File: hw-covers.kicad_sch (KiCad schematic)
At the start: 110 parts, among them J1 Screw_Terminal_01x02, J2 Screw_Terminal_01x10, J3 Conn_01x04_Pin, J4 Conn_01x04_Pin, J5 Screw_Terminal_01x15, K1 JRC-21F(4100), K10 JRC-21F(4100), K2 JRC-21F(4100), K3 JRC-21F(4100), K4 JRC-21F(4100), K5 JRC-21F(4100), K6 JRC-21F(4100), K7 JRC-21F(4100), K8 JRC-21F(4100), K9 JRC-21F(4100), Q1 PMBT3904235, Q10 PMBT3904235, Q11 PMBT3904235, Q2 PMBT3904235, Q3 PMBT3904235, Q4 PMBT3904235, Q5 PMBT3904235, Q6 PMBT3904235, Q7 PMBT3904235, Q8 PMBT3904235, Q9 PMBT3904235, SW1 SW_Push, U2 NCP1117-3.3_SOT223, U3 HLK-2M05, U4 ESP32-S3-WROOM-1

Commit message: Release 1.0
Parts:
- removed D14: LED, LED_THT:LED_D5.0mm, symbol Device:LED
- removed J1: Screw_Terminal_01x02, Connector_Phoenix_MSTB:PhoenixContact_MSTBA_2,5_2-G_1x02_P5.00mm_Horizontal, symbol Connector:Screw_Terminal_01x02
- removed J2: Screw_Terminal_01x10, Connector_Phoenix_MSTB:PhoenixContact_MSTBA_2,5_10-G_1x10_P5.00mm_Horizontal, symbol Connector:Screw_Terminal_01x10
- removed J5: Screw_Terminal_01x15, Connector_Phoenix_MC:PhoenixContact_MC_1,5_15-G-3.81_1x15_P3.81mm_Horizontal, symbol Connector:Screw_Terminal_01x15
- removed U4: ESP32-S3-WROOM-1, RF_Module:ESP32-S3-WROOM-1, symbol RF_Module:ESP32-S3-WROOM-1
- added J1, J2, J7: Screw_Terminal_01x04, Connector_Phoenix_MSTB:PhoenixContact_MSTBA_2,5_4-G-5,08_1x04_P5.08mm_Horizontal, symbol Connector:Screw_Terminal_01x04
- added J10, J11, J5, J8, J9: Screw_Terminal_01x03, Connector_Phoenix_MC:PhoenixContact_MC_1,5_3-G-3.81_1x03_P3.81mm_Horizontal, symbol Connector:Screw_Terminal_01x03
- added J6: Conn_01x02_Pin, Connector_PinHeader_2.54mm:PinHeader_1x02_P2.54mm_Vertical, symbol Connector:Conn_01x02_Pin
- added TP1, TP2: TestPoint, TestPoint:TestPoint_Pad_D1.5mm, symbol Connector:TestPoint
- added U1: ESP32-S3-WROOM-1, guille-lib:ESP32-S3-WROOM-1, symbol guille-lib:ESP32-S3-WROOM-1
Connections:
- net +3V3: now also U1.2 (3V3)
- net 1IN1: now also U1.22 (IO14)
- net 1IN2: now also U1.23 (IO21)
- net 1OUT1: now also U1.9 (IO16)
- net 1OUT2: now also U1.10 (IO17)
- net 2IN1: now also U1.24 (IO47)
- net 2IN2: now also U1.25 (IO48)
- net 2OUT1: now also U1.11 (IO18)
- net 2OUT2: now also U1.12 (IO8)
- net 3IN1: now also U1.32 (IO39)
- net 3IN2: now also U1.33 (IO40)
- net 3OUT1: now also U1.13 (USB_D-)
- net 3OUT2: now also U1.14 (USB_D+)
- net 4IN1: now also U1.34 (IO41)
- net 4IN2: now also U1.35 (IO42)
- net 4OUT1: now also U1.17 (IO9)
- net 4OUT2: now also U1.18 (IO10)
- net 5IN1: now also U1.38 (IO2)
- net 5IN2: now also U1.39 (IO1)
- net 5OUT1: now also U1.19 (IO11)
- net 5OUT2: now also U1.20 (IO12)
- net ESP_IO0: now also U1.27 (IO0)
- net ESP_RX: now also J4.2 (Pin_2), U1.36 (RXD0); no longer J4.3 (Pin_3)
- net ESP_TX: now also J4.3 (Pin_3), U1.37 (TXD0); no longer J4.2 (Pin_2)
- net EXT1: now also U1.5 (IO5)
- net EXT2: now also U1.4 (IO4)
- net GND: now also J10.3 (Pin_3), J11.3 (Pin_3), J5.3 (Pin_3), J8.3 (Pin_3), J9.3 (Pin_3), U1.1 (GND), U1.40 (GND), U1.41 (GND)
- net IN1_DOWN: now also J5.2 (Pin_2)
- net IN1_UP: now also J5.1 (Pin_1)
- net IN2_DOWN: now also J8.2 (Pin_2)
- net IN2_UP: now also J8.1 (Pin_1)
- net IN3_DOWN: now also J9.2 (Pin_2)
- net IN3_UP: now also J9.1 (Pin_1)
- net IN4_DOWN: now also J10.2 (Pin_2)
- net IN4_UP: now also J10.1 (Pin_1)
- net IN5_DOWN: now also J11.2 (Pin_2)
- net IN5_UP: now also J11.1 (Pin_1)
- net IR: now also U1.6 (IO6)
- net L: now also J2.4 (Pin_4)
- net LED1: now also U1.8 (IO15)
- net LED2: now also U1.7 (IO7)
- net N: now also J2.3 (Pin_3)
- net OUT1_DOWN: now also J7.2 (Pin_2)
- net OUT1_UP: now also J7.1 (Pin_1)
- net OUT2_DOWN: now also J7.4 (Pin_4)
- net OUT2_UP: now also J7.3 (Pin_3)
- net OUT3_DOWN: now also J1.2 (Pin_2)
- net OUT3_UP: now also J1.1 (Pin_1)
- net OUT4_DOWN: now also J1.4 (Pin_4)
- net OUT4_UP: now also J1.3 (Pin_3)
- net OUT5_DOWN: now also J2.2 (Pin_2)
- net OUT5_UP: now also J2.1 (Pin_1)
- net at R4.1: now also U1.3 (EN)
- net at Q11.3: now also J6.2 (Pin_2)
- net at R17.2: now also J6.1 (Pin_1)
- new net: TP1.1, U1.21 (IO13)
- new net: TP2.1, U1.31 (IO38)
- no-connect marks 22 -> 20
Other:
- company: (none) -> Guille González
- title: (none) -> Covers
- moved on the sheet: Q11, R17

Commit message: Release 1.1
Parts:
- removed K1, K10, K2, K3, K4, K5, K6, K7, K8, K9: JRC-21F(4100), guille-lib:JRC-21F(4100), symbol guille-lib:JRC-21F(4100)
- removed R16: 1k, Resistor_SMD:R_0402_1005Metric, symbol Device:R
- removed U3: HLK-2M05, guille-lib:HLK-2M05, symbol guille-lib:HLK-2M05
- added K1, K10, K2, K3, K4, K5, K6, K7, K8, K9: HF46F, guille-lib:HF46F, symbol guille-lib:HF46F
- added PS1: HLK-2M05, Converter_ACDC:Converter_ACDC_Hi-Link_HLK-2Mxx, symbol Converter_ACDC:HLK-2M05
- added R5: 1k, Resistor_SMD:R_0603_1608Metric, symbol Device:R
- C1, C2: footprint Capacitor_SMD:C_1206_3216Metric -> Capacitor_SMD:C_0805_2012Metric
- C10, C11, C12, C13, C14, C4, C5, C6, C7, C8, C9: footprint Capacitor_SMD:C_0402_1005Metric -> Capacitor_SMD:C_0603_1608Metric
- D1, D10, D11, D12, D13, D2, D6, D7, D8, D9: footprint Diode_SMD:D_SOD-323 -> Diode_SMD:D_SOD-123
- R1, R10, R11, R12, R13, R14, R15, R18, R19, R2, R20, R21, R22, R23, R24, R25, R26, R27, R28, R29, R3, R30, R31, R32, R33, R34, R35, R36, R37, R4, R9: footprint Resistor_SMD:R_0402_1005Metric -> Resistor_SMD:R_0603_1608Metric
- R17: value 1k -> 180; footprint Resistor_SMD:R_0402_1005Metric -> Resistor_SMD:R_0603_1608Metric
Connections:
- net +5V: now also K1.4, K10.4, K2.4, K3.4, K4.4, K5.4, K6.4, K7.4, K8.4, K9.4, PS1.4 (+Vout)
- net 1OUT1: now also U1.18 (IO10); no longer U1.9 (IO16)
- net 1OUT2: now also R1.1, U1.17 (IO9); no longer R9.1, U1.10 (IO17)
- net 2OUT1: now also U1.14 (USB_D+), R5.1; no longer R1.1, U1.11 (IO18)
- net 2OUT2: now also R9.1, U1.13 (USB_D-); no longer R10.1, U1.12 (IO8)
- net 3OUT1: now also R10.1, U1.12 (IO8); no longer R11.1, U1.13 (USB_D-)
- net 3OUT2: now also R11.1, U1.11 (IO18); no longer R13.1, U1.14 (USB_D+)
- net 4OUT1: now also U1.10 (IO17); no longer U1.17 (IO9)
- net 4OUT2: now also R13.1, U1.9 (IO16); no longer R14.1, U1.18 (IO10)
- net 5OUT1: now also R14.1, U1.8 (IO15); no longer R15.1, U1.19 (IO11)
- net 5OUT2: now also R15.1, U1.7 (IO7); no longer U1.20 (IO12)
- net GND: now also PS1.3 (-Vout)
- net LED1: now also U1.19 (IO11); no longer U1.8 (IO15)
- net LED2: now also U1.20 (IO12); no longer U1.7 (IO7)
- net LF: now also K1.2, K10.2, K2.2, K3.2, K4.2, K5.2, K6.2, K7.2, K8.2, K9.2, PS1.1 (AC/L)
- net N: now also PS1.2 (AC/N)
- net OUT1_DOWN: now also J2.1 (Pin_1), K2.1; no longer J7.2 (Pin_2)
- net OUT1_UP: now also J2.2 (Pin_2), K1.1; no longer J7.1 (Pin_1)
- net OUT2_DOWN: now also J1.3 (Pin_3), K4.1; no longer J7.4 (Pin_4)
- net OUT2_UP: now also J1.4 (Pin_4), K3.1; no longer J7.3 (Pin_3)
- net OUT3_DOWN: now also J1.1 (Pin_1), K6.1; no longer J1.2 (Pin_2)
- net OUT3_UP: now also J1.2 (Pin_2), K5.1; no longer J1.1 (Pin_1)
- net OUT4_DOWN: now also J7.3 (Pin_3), K8.1; no longer J1.4 (Pin_4)
- net OUT4_UP: now also J7.4 (Pin_4), K7.1; no longer J1.3 (Pin_3)
- net OUT5_DOWN: now also J7.1 (Pin_1), K10.1; no longer J2.2 (Pin_2)
- net OUT5_UP: now also J7.2 (Pin_2), K9.1; no longer J2.1 (Pin_1)
- net at D2.2 (A), Q1.3: now also K1.3
- net at R9.2: now also Q4.1; no longer Q3.1
- net at D6.2 (A), Q3.3: now also K3.3
- net at Q10.1: now also R15.2
- net at D13.2 (A), Q10.3: now also K10.3
- net at Q6.1: now also R11.2; no longer R12.2
- net at Q9.1: now also R14.2; no longer R15.2
- net at D12.2 (A), Q9.3: now also K9.3
- net at Q5.1: now also R10.2; no longer R11.2
- net at D7.2 (A), Q4.3: now also K4.3
- net at D1.2 (A), Q2.3: now also K2.3
- net at Q8.1: now also R13.2; no longer R14.2
- net at D9.2 (A), Q6.3: now also K6.3
- net at Q7.1: now also R12.2; no longer R13.2
- net at D8.2 (A), Q5.3: now also K5.3
- net at D10.2 (A), Q7.3: now also K7.3
- net at D11.2 (A), Q8.3: now also K8.3
- new net: Q3.1, R5.2
- no-connect marks 20 -> 10
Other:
- note added: "R LED_IR: (5V-1.5V)/20mA = 175ohm 180ohm (commercial)"
- note removed: "TBD"
- moved on the sheet: D2, H1, H2, H3, H4, Q1, R2

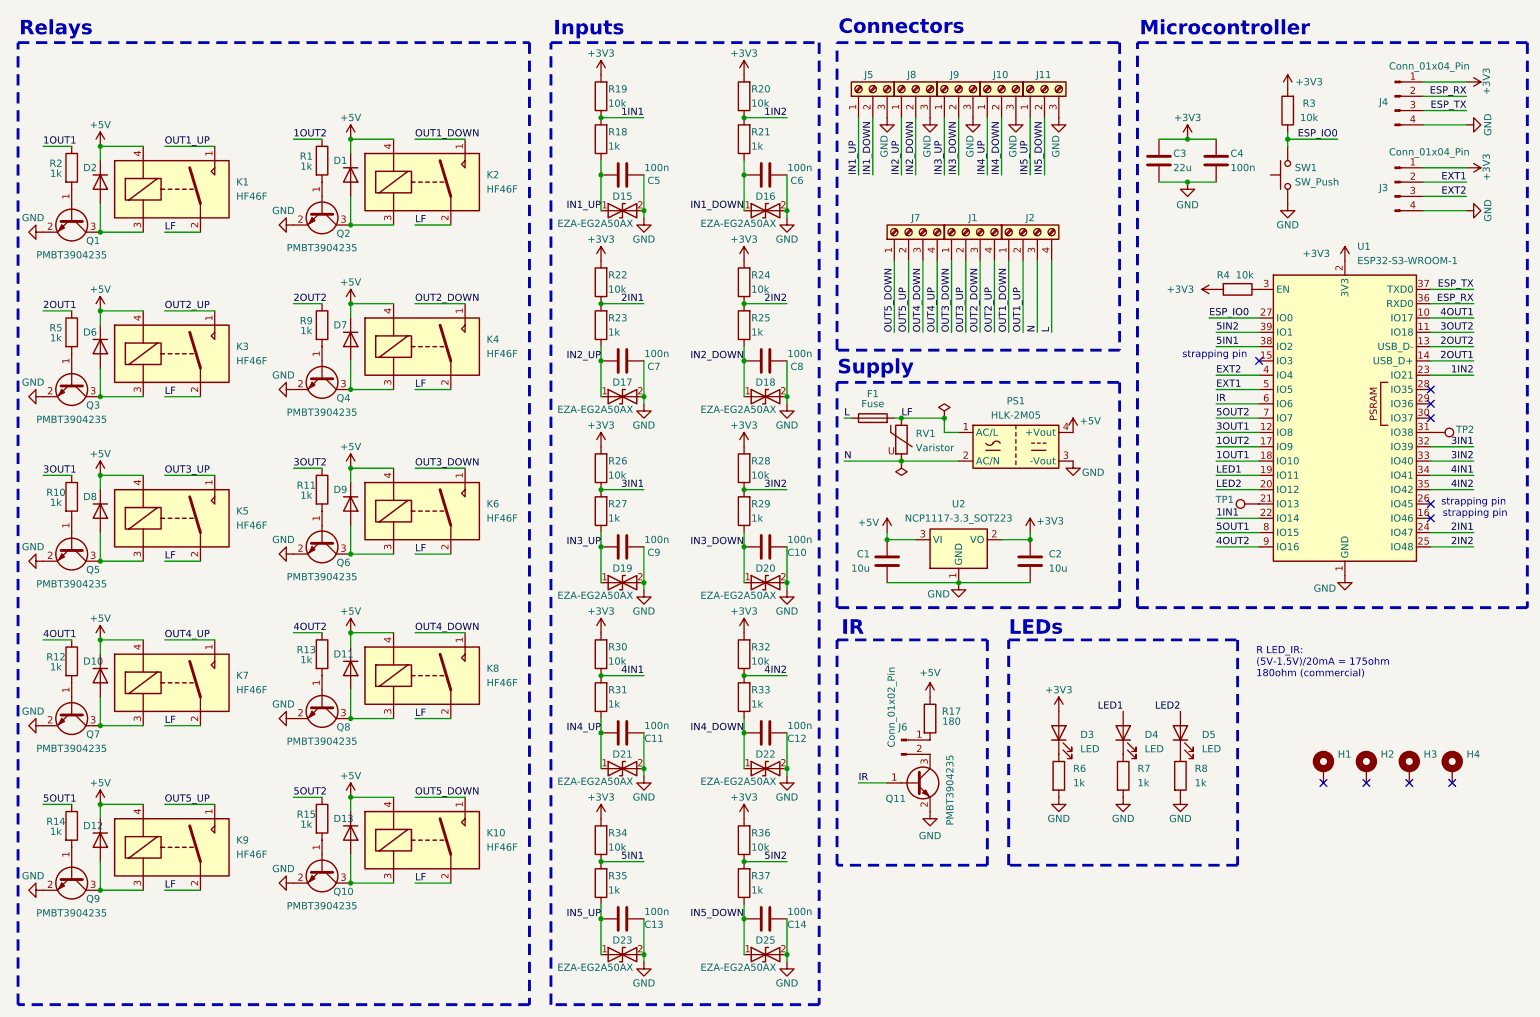
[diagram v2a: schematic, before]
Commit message: Sch update for rev 2
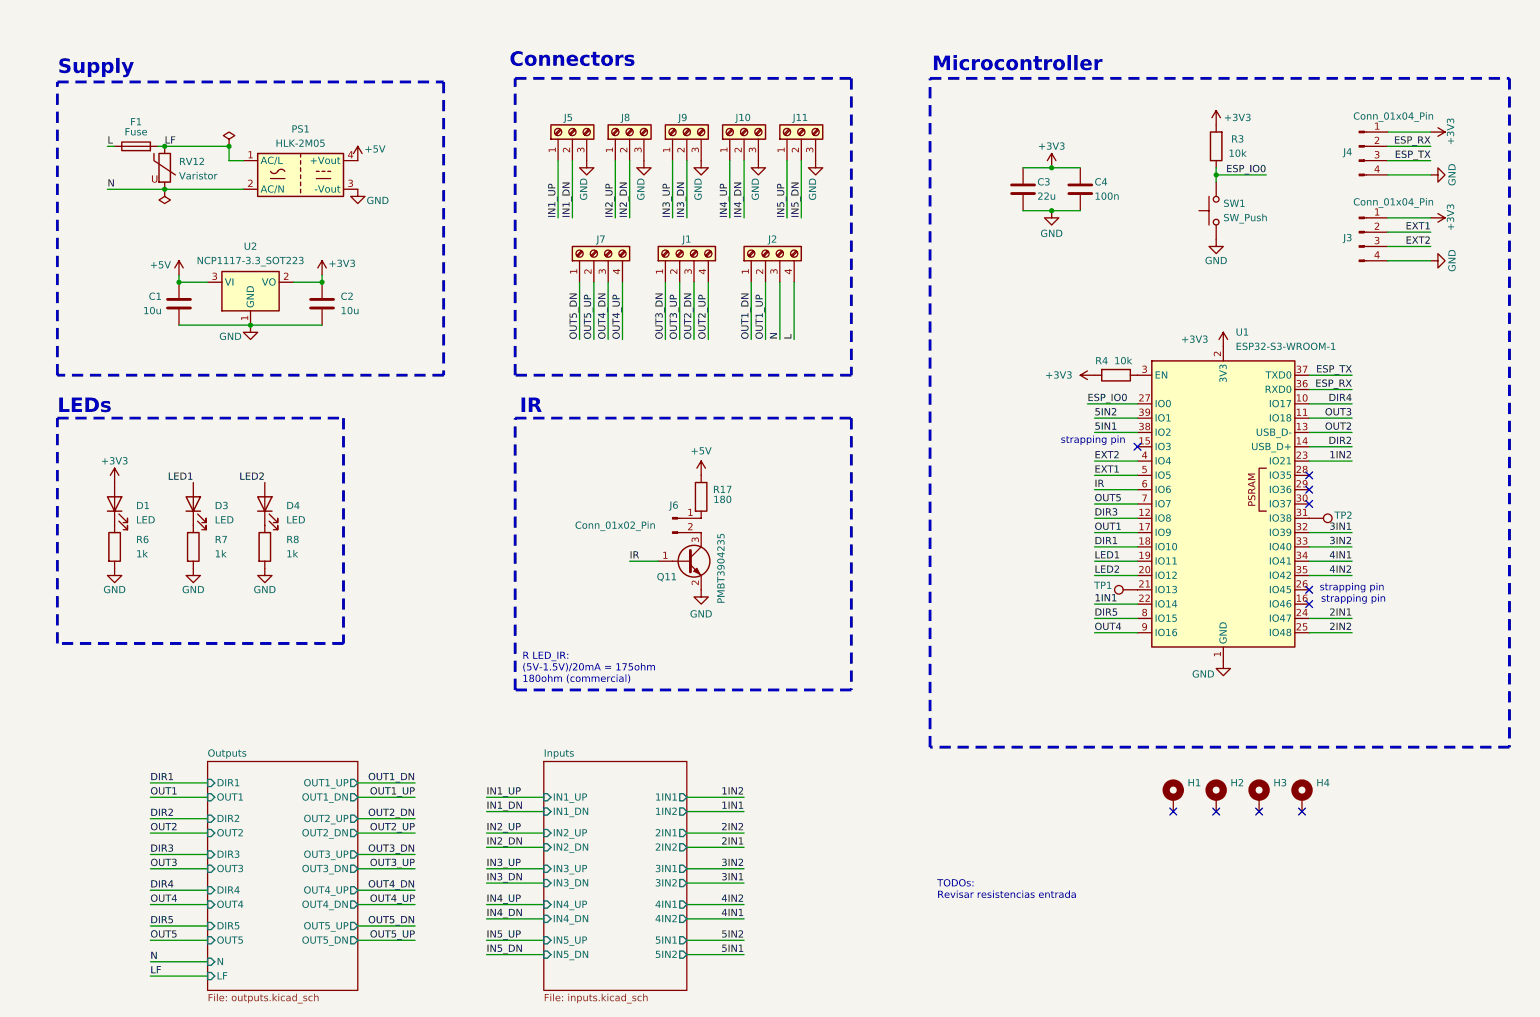
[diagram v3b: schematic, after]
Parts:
- removed C10, C11, C12, C13, C14, C5, C6, C7, C8, C9: 100n, Capacitor_SMD:C_0603_1608Metric, symbol Device:C
- removed D1, D10, D11, D12, D13, D2, D6, D7, D8, D9: 1N4448W, Diode_SMD:D_SOD-123, symbol Device:D
- removed D15, D16, D17, D18, D19, D20, D21, D22, D23, D25: EZA-EG2A50AX, guille-lib:EZAEG2A50AX, symbol guille-lib:EZA-EG2A50AX
- removed D5: LED, LED_SMD:LED_0603_1608Metric, symbol Device:LED
- removed K1, K10, K2, K3, K4, K5, K6, K7, K8, K9: HF46F, guille-lib:HF46F, symbol guille-lib:HF46F
- removed Q1, Q10, Q2, Q3, Q4, Q5, Q6, Q7, Q8, Q9: PMBT3904235, Package_TO_SOT_SMD:SOT-23, symbol guille-lib:PMBT3904235
- removed R1, R10, R11, R12, R13, R14, R15, R18, R2, R21, R23, R25, R27, R29, R31, R33, R35, R37, R5, R9: 1k, Resistor_SMD:R_0603_1608Metric, symbol Device:R
- removed R19, R20, R22, R24, R26, R28, R30, R32, R34, R36: 10k, Resistor_SMD:R_0603_1608Metric, symbol Device:R
- removed RV1: Varistor, Varistor:RV_Disc_D12mm_W4.5mm_P7.5mm, symbol Device:Varistor
- added D1: LED, LED_SMD:LED_0603_1608Metric, symbol Device:LED
- added RV12: Varistor, Varistor:RV_Disc_D12mm_W4.5mm_P7.5mm, symbol Device:Varistor
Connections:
- net +3V3: now also D1.2 (A); no longer D3.2 (A)
- net LED1: now also D3.2 (A); no longer D4.2 (A)
- net LED2: now also D4.2 (A)
- net LF: now also RV12.1
- net N: now also RV12.2
- net at R6.1: now also D1.1 (K); no longer D3.1 (K)
- net at R8.1: now also D4.1 (K)
- net at R7.1: now also D3.1 (K); no longer D4.1 (K)
- net 1OUT1 renamed DIR1
- net 1OUT2 renamed OUT1
- net 2OUT1 renamed DIR2
- net 2OUT2 renamed OUT2
- net 3OUT1 renamed DIR3
- net 3OUT2 renamed OUT3
- net 4OUT1 renamed DIR4
- net 4OUT2 renamed OUT4
- net 5OUT1 renamed DIR5
- net 5OUT2 renamed OUT5
- net IN1_DOWN renamed IN1_DN
- net IN2_DOWN renamed IN2_DN
- net IN3_DOWN renamed IN3_DN
- net IN4_DOWN renamed IN4_DN
- net IN5_DOWN renamed IN5_DN
- net OUT1_DOWN renamed OUT1_DN
- net OUT2_DOWN renamed OUT2_DN
- net OUT3_DOWN renamed OUT3_DN
- net OUT4_DOWN renamed OUT4_DN
- net OUT5_DOWN renamed OUT5_DN
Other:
- added sheet Inputs (inputs.kicad_sch)
- added sheet Outputs (outputs.kicad_sch)
- note added: "TODOs: Revisar resistencias entrada"
- note removed: "Inputs"
- note removed: "Relays"
- moved on the sheet: C1, C2, C3, C4, F1, H1, H2, H3, H4, J1, J10, J11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

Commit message: Change in R values and routing test
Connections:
- net OUT1_DN: now also J2.2 (Pin_2); no longer J2.1 (Pin_1)
- net OUT1_UP: now also J2.1 (Pin_1); no longer J2.2 (Pin_2)
- net OUT2_DN: now also J1.4 (Pin_4); no longer J1.3 (Pin_3)
- net OUT2_UP: now also J1.3 (Pin_3); no longer J1.4 (Pin_4)
- net OUT3_DN: now also J1.2 (Pin_2); no longer J1.1 (Pin_1)
- net OUT3_UP: now also J1.1 (Pin_1); no longer J1.2 (Pin_2)
- net OUT4_DN: now also J7.4 (Pin_4); no longer J7.3 (Pin_3)
- net OUT4_UP: now also J7.3 (Pin_3); no longer J7.4 (Pin_4)
- net OUT5_DN: now also J7.2 (Pin_2); no longer J7.1 (Pin_1)
- net OUT5_UP: now also J7.1 (Pin_1); no longer J7.2 (Pin_2)
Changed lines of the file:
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@@
 	)
 	(label "OUT3_UP"
-		(at 132.08 71.12 90)
+		(at 129.54 71.12 90)
 		(effects
 			(font
@@
 	)
 	(label "OUT4_UP"
-		(at 121.92 71.12 90)
+		(at 119.38 71.12 90)
 		(effects
 			(font
@@
 	)
 	(label "OUT5_UP"
-		(at 116.84 71.12 90)
+		(at 114.3 71.12 90)
 		(effects
 			(font
@@
 	)
 	(label "OUT3_DN"
-		(at 129.54 71.12 90)
+		(at 132.08 71.12 90)
 		(effects
 			(font
@@
 	)
 	(label "OUT2_DN"
-		(at 134.62 71.12 90)
+		(at 137.16 71.12 90)
 		(effects
 			(font
@@
 	)
 	(label "OUT4_DN"
-		(at 119.38 71.12 90)
+		(at 121.92 71.12 90)
 		(effects
 			(font
@@
 	)
 	(label "OUT1_DN"
-		(at 144.78 71.12 90)
+		(at 147.32 71.12 90)
 		(effects
 			(font
@@
 	)
 	(label "OUT1_UP"
-		(at 147.32 71.12 90)
+		(at 144.78 71.12 90)
 		(effects
 			(font
@@
 	)
 	(label "OUT5_DN"
-		(at 114.3 71.12 90)
+		(at 116.84 71.12 90)
 		(effects
 			(font
@@
 	)
 	(label "OUT2_UP"
-		(at 137.16 71.12 90)
-		(effects
-			(font
+		(at 134.62 71.12 90)
+		(effects
+			(font
